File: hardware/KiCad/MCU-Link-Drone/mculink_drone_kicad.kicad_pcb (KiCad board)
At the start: 2 copper layers, 60.7 x 43 mm, 109 parts, among them J1 Conn_01x10, J3 Jumper_2_Open, J4 Jumper_2_Open, J5 Jumper_2_Open, J6 Conn_02x05_Odd_Even, J7 1x3pos, 100mil pitch, J8 Conn_01x04_Male, J9 USB4110-GF-A_REVB, SW1 KMR221GLFS, U1 LPC55S69JBD64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

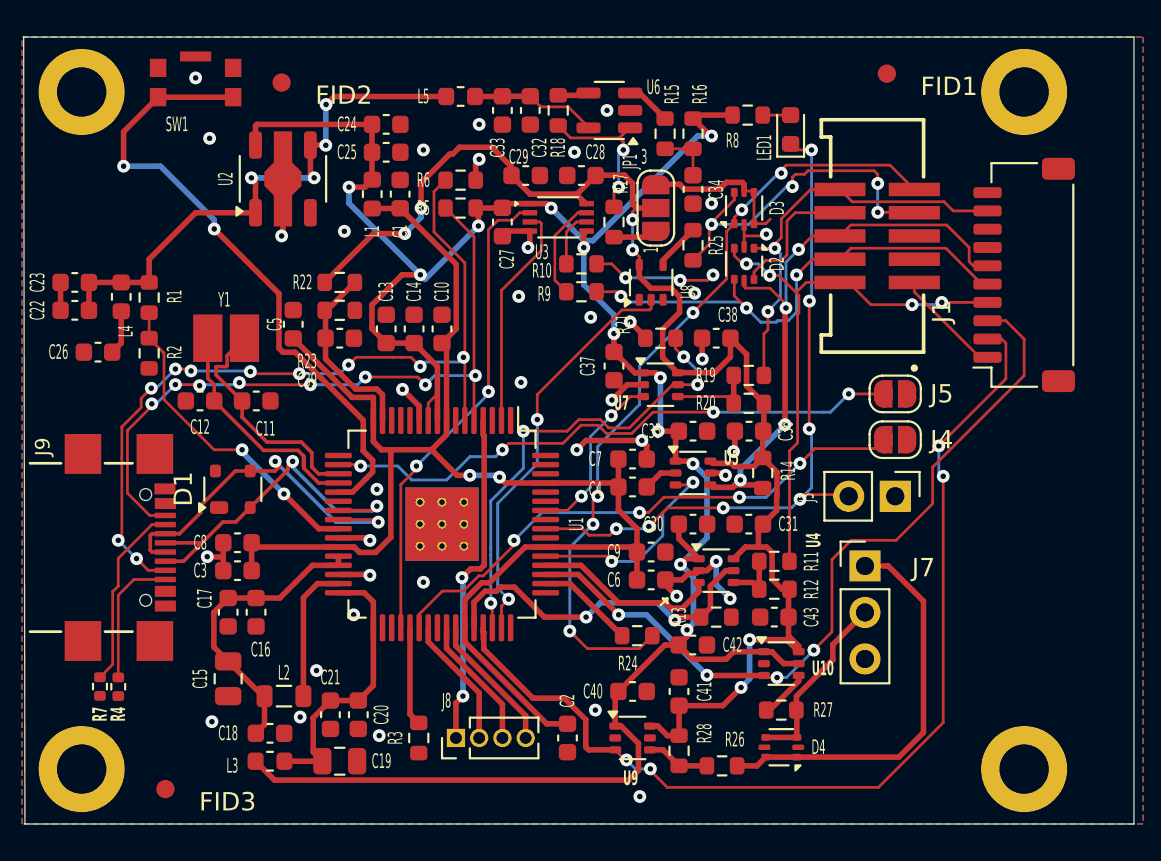
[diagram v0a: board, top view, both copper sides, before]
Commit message: fixed warnings
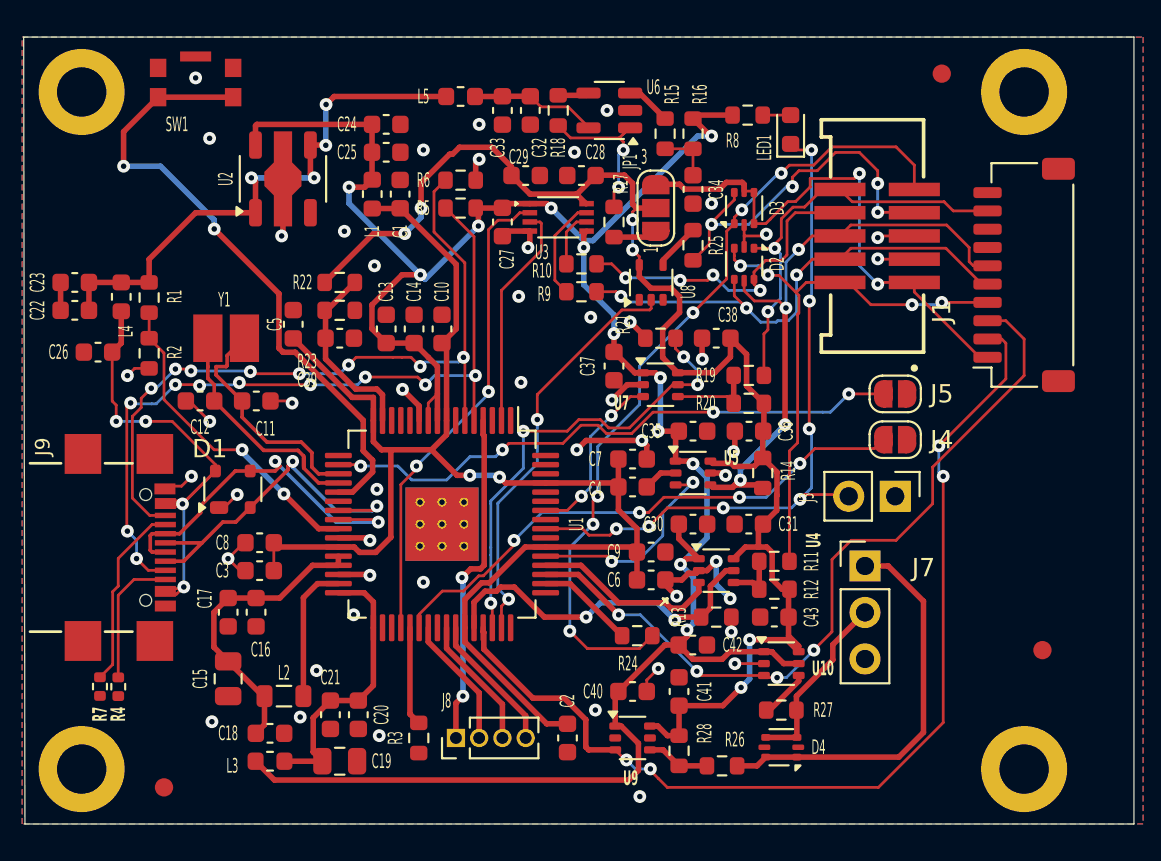
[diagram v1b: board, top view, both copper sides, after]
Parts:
- moved FID3 57.7 mm to (214.0, 78.0)
- moved FID1 55.5 mm to (171.5, 117.0)
- moved FID2 51.9 mm to (219.5, 109.5)
- moved C3 1.21 mm to (176.7, 105.2)
- moved C8 1.21 mm to (176.7, 103.6)
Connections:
- J1 pad MP: (no net) -> unconnected-(J1-PadMP)
- J9 pad A1: (no net) -> GND
- J9 pad A12: (no net) -> GND
- J9 pad A4: (no net) -> /McuLink Power and USB/USB_VBUS
- J9 pad A8: LPC_SWDCLK -> LPC_SWDIO
- J9 pad A9: (no net) -> /McuLink Power and USB/USB_VBUS
- J9 pad B1: (no net) -> GND
- J9 pad B12: (no net) -> GND
- J9 pad B4: (no net) -> /McuLink Power and USB/USB_VBUS
- J9 pad B8: LPC_SWDIO -> LPC_SWDCLK
- J9 pad B9: (no net) -> /McuLink Power and USB/USB_VBUS
- J9 pad S1: GND -> unconnected-(J9-SHIELD-PadS1)_1
- U8 pad 1: (no net) -> unconnected-(U8-NC-Pad1)
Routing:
- net /McuLink Power and USB/USB_VBUS: track 2.55 -> 26.9 mm, vias 0 -> 4
- net GND: track 38.8 -> 54.2 mm, vias 39 -> 49
- net /Debug interface/VTARGET: track 14.8 -> 29.4 mm, vias 0 -> 2
- net LPC_SWDIO: track 39.1 -> 42.9 mm, vias 8 -> 10
- net LPC_SWDCLK: track 44.9 -> 41.2 mm, vias 10 -> 8
- net /Debug interface/IF_TDI: track 14.4 -> 18.1 mm, vias 3 -> 4
- net /Debug interface/IF_DETECT: track 43.2 -> 44.7 mm
- net /McuLink Power and USB/MCU_VDDIO: track 81.3 -> 80.1 mm
- net /Debug interface/IF_ISPEN: track 20.6 -> 21.5 mm

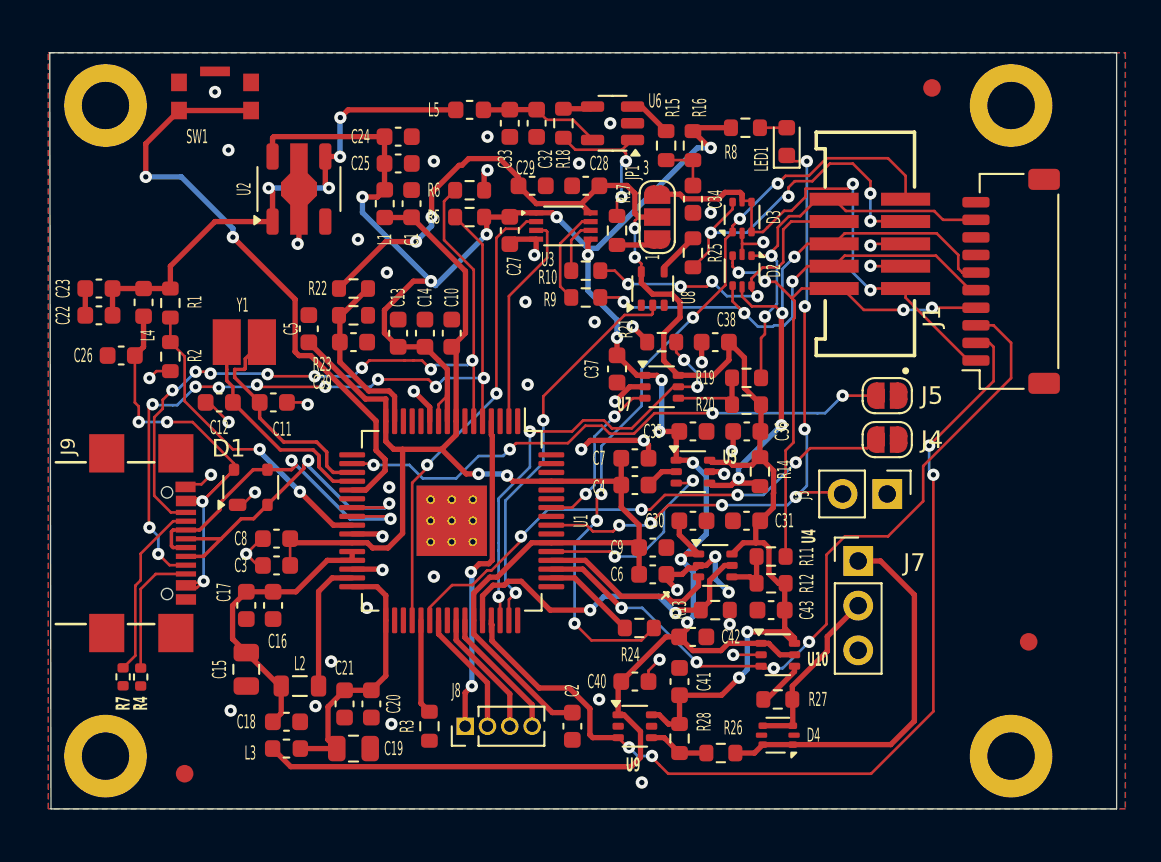
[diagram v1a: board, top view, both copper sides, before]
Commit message: added 3D models
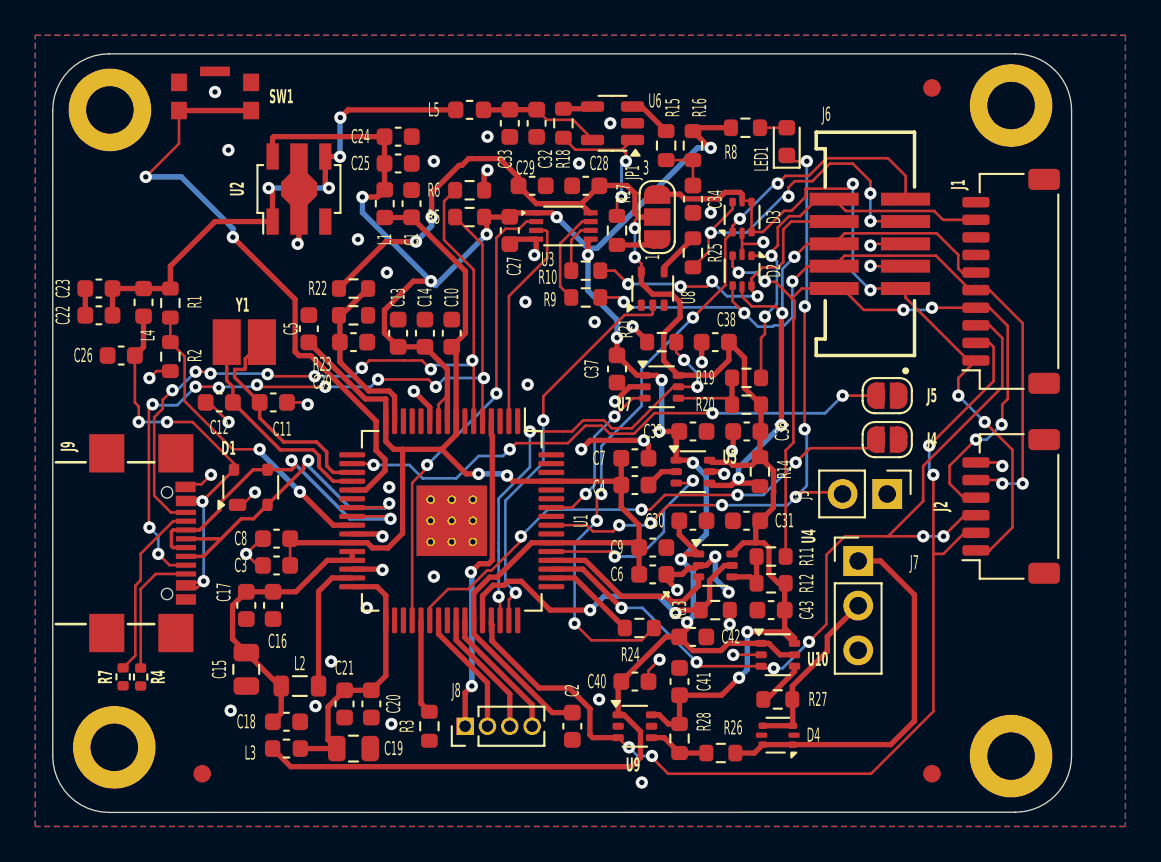
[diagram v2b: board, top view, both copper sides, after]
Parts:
- added J2: Pixhawk_Debug_Mini, McuOnEclipse:JST_SH_SM06B-SRSS-TB_1x06-1MP_P1.00mm_Horizontal, F.Cu at (218.5, 101.8)
- added L6: Logo HSLU, McuOnEclipse:Hochschule_Luzern_New, B.Cu at (193.5, 79.5)
- added L7: Logo HSLU, McuOnEclipse:Hochschule_Luzern_Small, B.Cu at (191.0, 109.5)
- J1: footprint Connector_JST:JST_SH_SM10B-SRSS-TB_1x10-1MP_P1.00mm_Horizontal -> McuOnEclipse:JST_SH_SM10B-SRSS-TB_1x10-1MP_P1.00mm_Horizontal
- SW1: footprint mculink_kicad:SW_C_K_KMR2 -> McuOnEclipse:SW_C_K_KMR2
- U2: footprint Package_TO_SOT_SMD:SOT-89-5 -> McuOnEclipse:SOT-89-5
- Y1: footprint mculink_kicad:CX3225GA16000D0PTVCC -> McuOnEclipse:CX3225GA16000D0PTVCC
- moved FID2 9.30 mm to (214.0, 117.0)
- moved FID1 1.00 mm to (172.5, 117.0)
- moved H3 0.71 mm to (167.5, 115.5)
- moved H1 0.35 mm to (167.2, 79.2)
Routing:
- net /Debug interface/IF_SWDIO: track 31.0 -> 46.5 mm, vias 4 -> 6
- net /Debug interface/IF_SWCLK: track 27.6 -> 42.7 mm, vias 3 -> 5
- net /Debug interface/VTARGET: track 29.4 -> 43.8 mm, vias 2 -> 4
- net FCO_TARGET_TXD: track 43.2 -> 49.0 mm, vias 4 -> 6
- net FC0_TARGET_RXD: track 55.2 -> 58.9 mm
- net GND: track 54.2 -> 55.7 mm, vias 49 -> 50
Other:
- board size 60.7 x 43 mm -> 57.9 x 43.1 mm

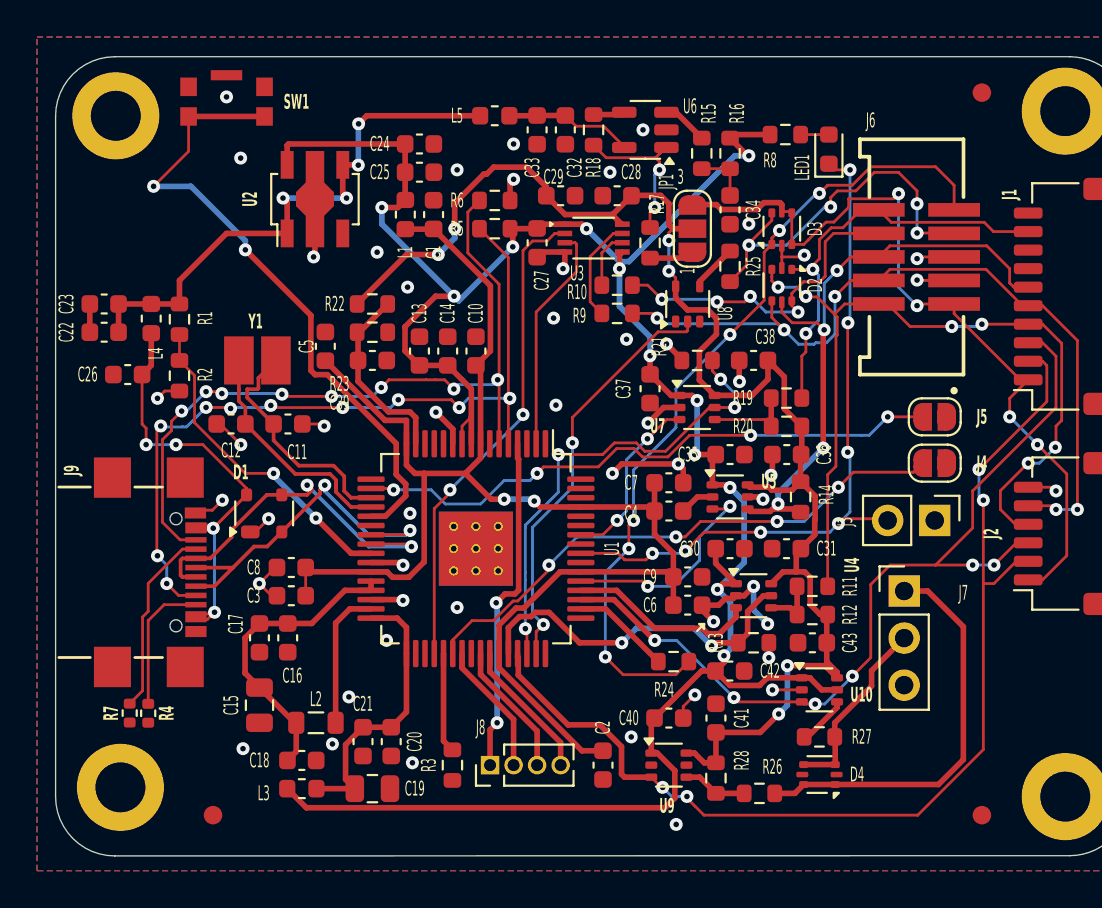
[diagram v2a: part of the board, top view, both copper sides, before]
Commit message: fixed warnings
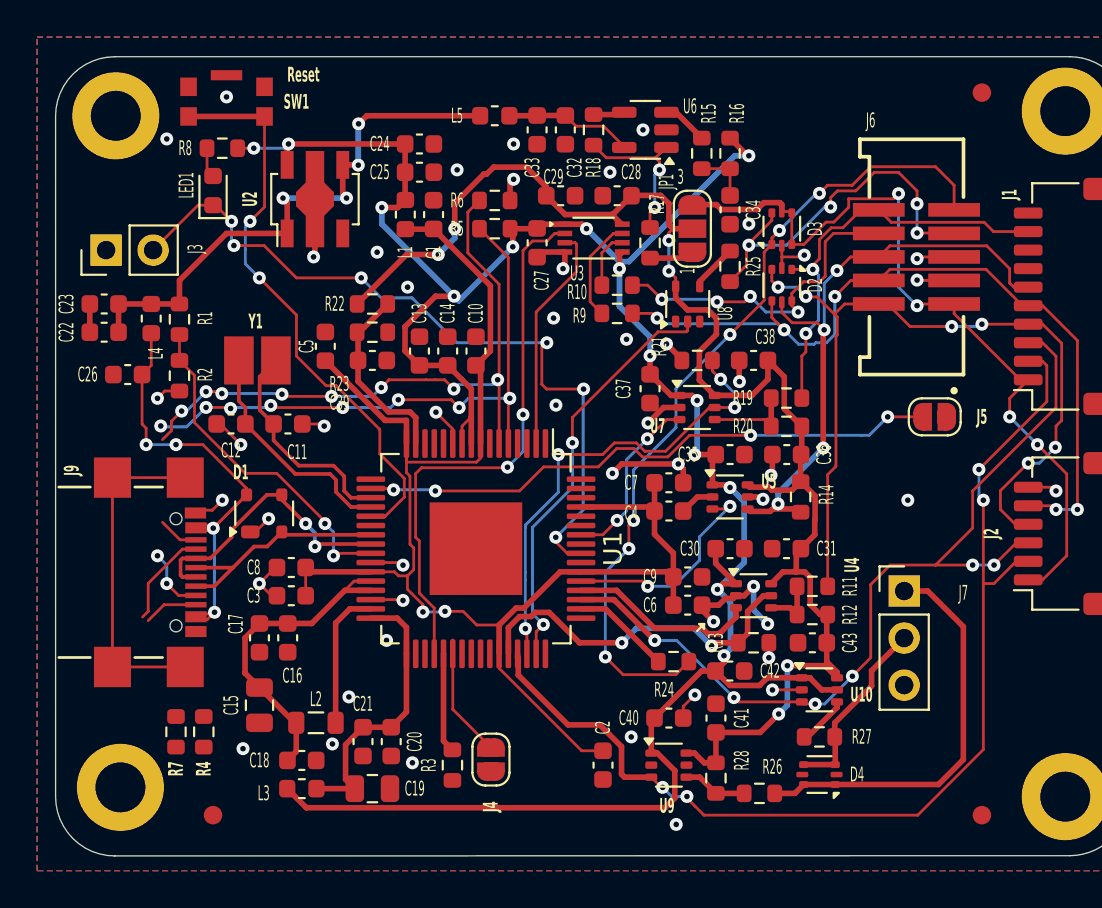
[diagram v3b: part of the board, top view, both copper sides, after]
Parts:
- removed J8: Conn_01x04_Male, Connector_PinHeader_1.27mm:PinHeader_1x04_P1.27mm_Vertical
- R4, R7: footprint Resistor_SMD:R_0402_1005Metric -> Resistor_SMD:R_0603_1608Metric
- U1: footprint Package_QFP:LQFP-64-1EP_10x10mm_P0.5mm_EP6.5x6.5mm_ThermalVias -> McuOnEclipse:LQFP-64-1EP_10x10mm_P0.5mm_EP5x5mm
- moved J3 47.0 mm to (166.7, 86.5), turned to 90 degrees
- moved LED1 33.3 mm to (172.5, 83.3)
- moved R8 30.4 mm to (173.0, 81.0), turned to 180 degrees
- moved J4 28.8 mm to (187.5, 114.0), turned to 90 degrees
- moved R4 3.16 mm to (172.0, 112.5)
- moved R7 2.70 mm to (170.5, 112.5)
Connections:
- U1 pad 39: Net-(J8-Pin_2) -> unconnected-(U1D-PIO1_1-Pad39)
- U1 pad 4: Net-(J8-Pin_1) -> unconnected-(U1D-PIO1_0-Pad4)
- U1 pad 41: Net-(J8-Pin_3) -> unconnected-(U1D-PIO1_2-Pad41)
- U1 pad 42: Net-(J8-Pin_4) -> unconnected-(U1D-PIO1_3-Pad42)
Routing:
- net HW_VER_6: track 30.5 -> 6.65 mm, vias 4 -> 0
- net Net-(J8-Pin_1): track 18.4 -> 0.00 mm, vias 2 -> 0
- net unconnected-(J9-SHIELD-PadS1): track 0.00 -> 18.1 mm
- net Net-(J8-Pin_4): track 7.60 -> 0.00 mm
- net Net-(J8-Pin_3): track 7.29 -> 0.00 mm
- net Net-(J8-Pin_2): track 7.17 -> 0.00 mm
- net /McuLink Power and USB/USB_D+: track 19.5 -> 12.7 mm, vias 2 -> 0
- net LPC_SWDIO: track 42.9 -> 36.1 mm
- net Net-(J9-CC1): track 10.2 -> 5.28 mm
- net /McuLink Power and USB/USB_D-: track 20.2 -> 15.4 mm
- net Net-(J9-CC2): track 7.42 -> 2.93 mm
- net LPC_SWDCLK: track 41.2 -> 36.7 mm
- net LPC_RST: track 34.9 -> 31.2 mm
- net DBGIF_TCK_SWCLK: track 26.4 -> 29.9 mm
- net PIO0_5-ISP_EN-LED1_CTRL: track 38.4 -> 41.4 mm, vias 7 -> 6
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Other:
- board text added: "Reset"

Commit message: improved layout
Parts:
- J4, J5: moved to B.Cu
- U1: footprint McuOnEclipse:LQFP-64-1EP_10x10mm_P0.5mm_EP5x5mm -> McuOnEclipse:LQFP-64-1EP_10x10mm_P0.5mm_EP3.5x3.5mm
- moved J5 32.6 mm to (179.0, 99.0), turned to 0 degrees
- moved J4 2.83 mm to (185.5, 112.0)
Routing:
- net HW_VER_7: track 31.9 -> 4.03 mm, vias 4 -> 1
- net unconnected-(J9-SHIELD-PadS1)_0: track 18.1 -> 0.00 mm
- net LPC_SWDIO: track 36.1 -> 43.0 mm
- net Net-(J9-CC1): track 5.28 -> 11.4 mm
- net Net-(J9-CC2): track 2.93 -> 7.55 mm
- net LPC_SWDCLK: track 36.7 -> 41.2 mm
- net HW_VER_6: track 6.65 -> 3.90 mm, vias 0 -> 1
- net GND: vias 49 -> 52
